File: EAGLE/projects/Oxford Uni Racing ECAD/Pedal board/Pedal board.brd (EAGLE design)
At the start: 165.1 x 114 mm, 50 parts, among them IC1 AD711N, J1 ASS + BOTS, J2 THR_1_2, J3 PWR_CAN, J6 BR_POS_PRESS_STWH, J7 T821108A1S100CEU, K2 EC2-12TNU, T1 BT169, X2 D-SUB9-H2M09ST

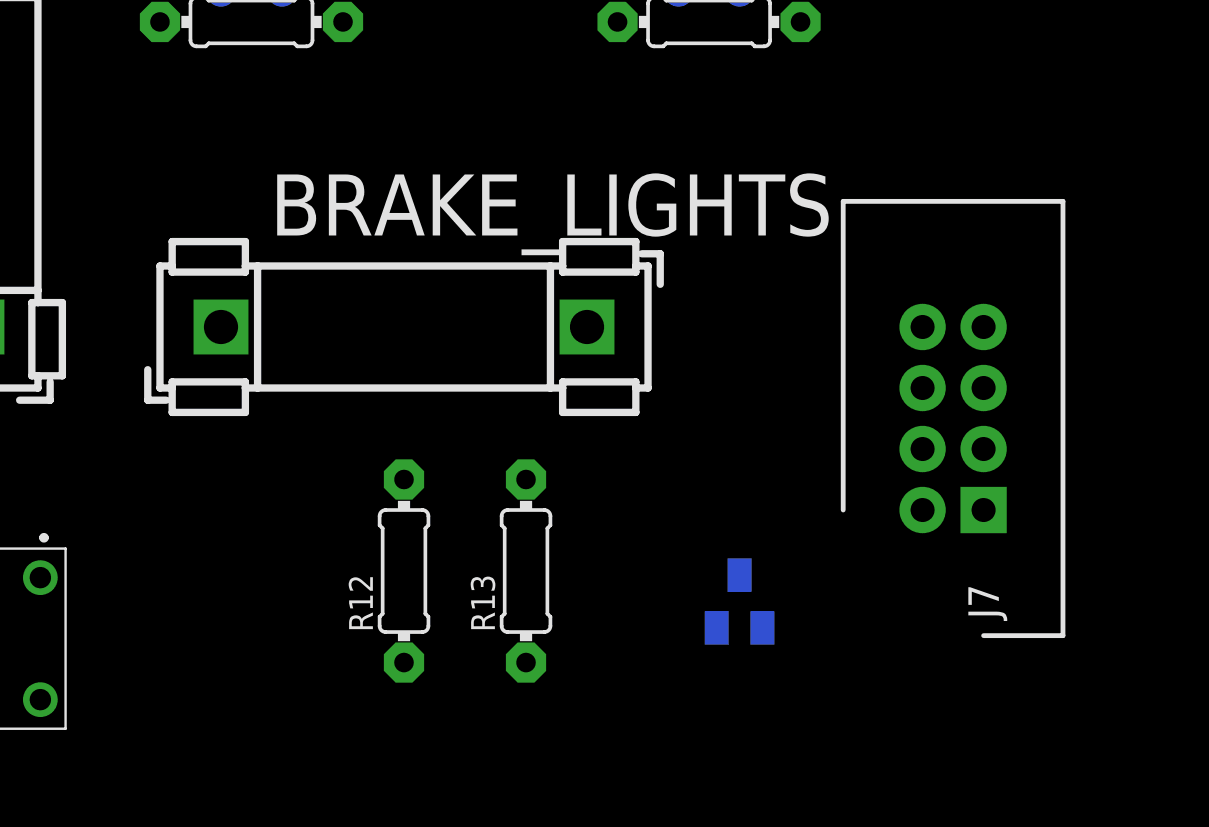
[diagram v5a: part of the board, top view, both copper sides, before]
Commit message: removed brake lights from pedal board
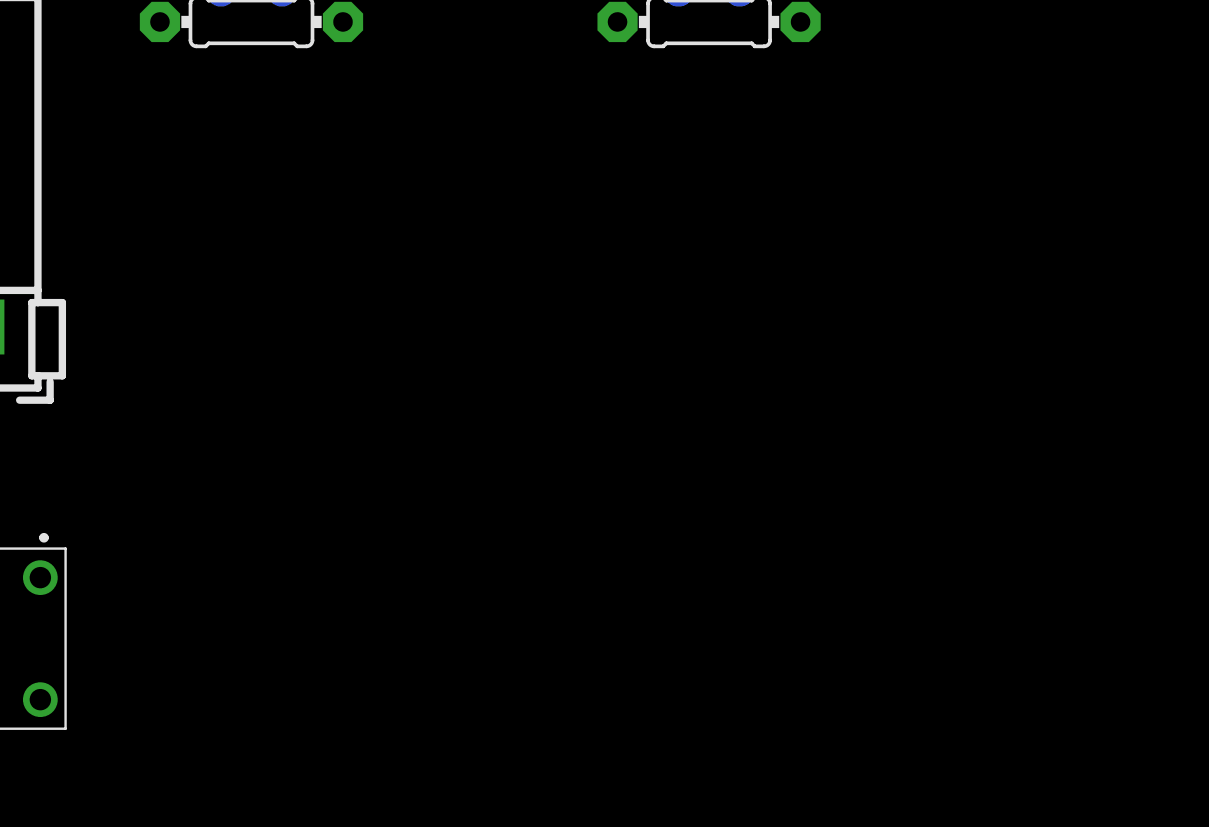
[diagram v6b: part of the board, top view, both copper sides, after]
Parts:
- removed BRAKE_LIGHTS: 1A, fuse:FUSE_HOLDER_5X20MM
- removed BR_LIGHTS_TR: IRLML2502GTRPBF, adafruit:SOT23
- removed J7: T821108A1S100CEU, T821108A1S100CEU:HDRV8W64P254_2X4_1778X895X915P
- removed R12: 1K, adafruit:0204/7
- removed R13: 47K, adafruit:0204/7
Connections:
- removed net 12V_BR_LIGHTS: BRAKE_LIGHTS.2, J7.8
- removed net BRAKE_LIGHTS_OUT: R12.1, U$1.J804-2
- removed net N$25: BR_LIGHTS_TR.1, R12.2, R13.2
- removed net N$28: BR_LIGHTS_TR.3, J7.3
- net 12V_BATTERY: no longer BRAKE_LIGHTS.1
- net BR_POSS2: no longer U$1.J803-3
- net GND: no longer BR_LIGHTS_TR.2, R13.1
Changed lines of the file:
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@@
 <attribute name="VALUE" x="85.09" y="24.13" size="1.27" layer="27" rot="R270" align="center"/>
-</element>
-<element name="J7" library="T821108A1S100CEU" package="HDRV8W64P254_2X4_1778X895X915P" value="T821108A1S100CEU" x="154.94" y="69.85" smashed="yes" rot="R90">
-<attribute name="DESCRIPTION" value="HEADER, VERTICAL, 2.54MM, 8WAY Amphenol T821 Series, 2.54mm Pitch 8 Way 2 Row Straight PCB Header, Solder Termination, 3A" x="154.94" y="67.31" size="1.778" layer="27" rot="R90" display="off"/>
-<attribute name="HEIGHT" value="9.15mm" x="154.94" y="67.31" size="1.778" layer="27" rot="R90" display="off"/>
-<attribute name="MANUFACTURER_NAME" value="Amphenol" x="154.94" y="67.31" size="1.778" layer="27" rot="R90" display="off"/>
-<attribute name="MANUFACTURER_PART_NUMBER" value="T821108A1S100CEU" x="154.94" y="67.31" size="1.778" layer="27" rot="R90" display="off"/>
-<attribute name="NAME" x="154.94" y="66.04" size="1.27" layer="25" rot="R90" align="center"/>
-<attribute name="RS_PART_NUMBER" value="1702738" x="154.94" y="67.31" size="1.778" layer="27" rot="R90" display="off"/>
-<attribute name="VALUE" x="157.48" y="73.66" size="1.27" layer="27" rot="R90" align="center"/>
-</element>
-<element name="R12" library="adafruit" library_urn="urn:adsk.eagle:library:420" package="0204/7" package3d_urn="urn:adsk.eagle:package:6240596/1" value="1K" x="130.81" y="67.31" smashed="yes" rot="R90">
-<attribute name="NAME" x="129.5146" y="64.77" size="0.9906" layer="25" ratio="12" rot="R90"/>
-<attribute name="VALUE" x="131.2926" y="65.6844" size="0.9906" layer="27" ratio="12" rot="R90"/>
-</element>
-<element name="R13" library="adafruit" library_urn="urn:adsk.eagle:library:420" package="0204/7" package3d_urn="urn:adsk.eagle:package:6240596/1" value="47K" x="135.89" y="67.31" smashed="yes" rot="R90">
-<attribute name="NAME" x="134.5946" y="64.77" size="0.9906" layer="25" ratio="12" rot="R90"/>
-<attribute name="VALUE" x="136.3726" y="65.6844" size="0.9906" layer="27" ratio="12" rot="R90"/>
-</element>
-<element name="BR_LIGHTS_TR" library="adafruit" library_urn="urn:adsk.eagle:library:420" package="SOT23" package3d_urn="urn:adsk.eagle:package:6240836/1" value="IRLML2502GTRPBF" x="144.78" y="66.04" smashed="yes" rot="MR0">
-<attribute name="NAME" x="146.685" y="67.945" size="1.27" layer="26" rot="MR0"/>
-<attribute name="VALUE" x="146.685" y="62.865" size="1.27" layer="28" rot="MR0"/>
 </element>
 <element name="IC1" library="analog-devices" library_urn="urn:adsk.eagle:library:102" package="DIL08" package3d_urn="urn:adsk.eagle:package:3915/1" value="AD711N" x="113.03" y="34.29" smashed="yes" rot="R270">
@@
 <attribute name="OC_NEWARK" value="unknown" x="113.03" y="77.47" size="1.778" layer="27" rot="R90" display="off"/>
 <attribute name="VALUE" x="131.318" y="2.032" size="2.54" layer="27" rot="R270"/>
-</element>
-<element name="BRAKE_LIGHTS" library="fuse" library_urn="urn:adsk.eagle:library:233" package="FUSE_HOLDER_5X20MM" package3d_urn="urn:adsk.eagle:package:14079/1" value="1A" x="123.19" y="77.47" smashed="yes">
-<attribute name="MF" value="" x="123.19" y="77.47" size="1.778" layer="27" display="off"/>
-<attribute name="MPN" value="" x="123.19" y="77.47" size="1.778" layer="27" display="off"/>
-<attribute name="NAME" x="125.222" y="81.28" size="2.54" layer="25"/>
-<attribute name="OC_FARNELL" value="unknown" x="123.19" y="77.47" size="1.778" layer="27" display="off"/>
-<attribute name="OC_NEWARK" value="unknown" x="123.19" y="77.47" size="1.778" layer="27" display="off"/>
-<attribute name="VALUE" x="124.968" y="71.628" size="2.54" layer="27"/>
 </element>
 <element name="R1" library="adafruit" library_urn="urn:adsk.eagle:library:420" package="0204/7" package3d_urn="urn:adsk.eagle:package:6240596/1" value="1M" x="104.14" y="43.18" smashed="yes">
@@
 <contactref element="J2" pad="4"/>
 <contactref element="J6" pad="3"/>
-<contactref element="R13" pad="1"/>
-<contactref element="BR_LIGHTS_TR" pad="2"/>
 <contactref element="IC1" pad="4"/>
 <contactref element="R17" pad="1"/>
@@
 <wire x1="186.18835" y1="29.21" x2="188.01714375" y2="26.57855625" width="0" layer="19" extent="16-16"/>
 <wire x1="182.88" y1="32.5657875" x2="182.88" y2="29.21" width="0" layer="19" extent="16-16"/>
-<wire x1="143.83" y1="64.94" x2="179.202075" y2="41.961225" width="0" layer="19" extent="16-16"/>
+<wire x1="144.78" y1="91.44" x2="180.161775" y2="42.920925" width="0" layer="19" extent="16-16"/>
+<wire x1="139.7" y1="90.17" x2="144.78" y2="91.44" width="0" layer="19" extent="16-16"/>
+<wire x1="134.62" y1="104.14" x2="144.78" y2="96.52" width="0" layer="19" extent="16-16"/>
+<wire x1="120.65" y1="90.17" x2="125.73" y2="91.44" width="0" layer="19" extent="16-16"/>
+<wire x1="99.06" y1="105.5624" x2="120.65" y2="90.17" width="0" layer="19" extent="1-1"/>
+<wire x1="87.63" y1="69.85" x2="93.98" y2="91.44" width="0" layer="19" extent="1-1"/>
+<wire x1="87.63" y1="62.23" x2="87.63" y2="69.85" width="0" layer="19" extent="1-1"/>
+<wire x1="87.63" y1="46.99" x2="87.63" y2="62.23" width="0" layer="19" extent="1-1"/>
+<wire x1="90.17" y1="46.99" x2="87.63" y2="46.99" width="0" layer="19" extent="1-1"/>
+<wire x1="87.63" y1="26.67" x2="87.63" y2="46.99" width="0" layer="19" extent="1-1"/>
+<wire x1="105.41" y1="31.75" x2="87.63" y2="26.67" width="0" layer="19" extent="1-1"/>
+<wire x1="109.22" y1="30.48" x2="105.41" y2="31.75" width="0" layer="19" extent="1-1"/>
+<wire x1="63.5" y1="60.96" x2="87.63" y2="62.23" width="0" layer="19" extent="1-1"/>
+<wire x1="63.5" y1="58.42" x2="63.5" y2="60.96" width="0" layer="19" extent="1-1"/>
 </signal>
 <signal name="N$7">
@@
 <wire x1="63.5" y1="45.72" x2="87.63" y2="24.13" width="0" layer="19" extent="1-1"/>
 </signal>
-<signal name="BRAKE_LIGHTS_OUT">
-<contactref element="R12" pad="1"/>
-<contactref element="U$1" pad="J804-2"/>
-<wire x1="15.24" y1="43.18" x2="130.81" y2="63.5" width="0" layer="19" extent="1-1"/>
-</signal>
-<signal name="N$25">
-<contactref element="R12" pad="2"/>
-<contactref element="R13" pad="2"/>
-<contactref element="BR_LIGHTS_TR" pad="1"/>
-<wire x1="135.89" y1="71.12" x2="145.73" y2="64.94" width="0" layer="19" extent="16-16"/>
-<wire x1="130.81" y1="71.12" x2="135.89" y2="71.12" width="0" layer="19" extent="1-1"/>
-</signal>
-<signal name="N$28">
-<contactref element="J7" pad="3"/>
-<contactref element="BR_LIGHTS_TR" pad="3"/>
-<wire x1="144.78" y1="67.14" x2="154.94" y2="72.39" width="0" layer="19" extent="16-16"/>
-</signal>
 <signal name="N$23">
 <contactref element="IC1" pad="6"/>
@@
 <contactref element="J6" pad="7"/>
 <contactref element="R4" pad="1"/>
-<contactref element="U$1" pad="J803-3"/>
 <wire x1="87.63" y1="21.59" x2="100.33" y2="17.78" width="0" layer="19" extent="1-1"/>
-<wire x1="63.5" y1="43.18" x2="87.63" y2="21.59" width="0" layer="19" extent="1-1"/>
 </signal>
 <signal name="ST_WH_POSS">
@@
 <contactref element="J3" pad="2"/>
 <contactref element="F1" pad="1"/>
-<contactref element="BRAKE_LIGHTS" pad="1"/>
-<wire x1="113.03" y1="77.47" x2="123.19" y2="77.47" width="0" layer="19" extent="1-1"/>
 <wire x1="91.44" y1="91.44" x2="113.03" y2="77.47" width="0" layer="19" extent="1-1"/>
 <wire x1="91.44" y1="93.98" x2="91.44" y2="91.44" width="0" layer="19" extent="1-1"/>
 </signal>
-<signal name="12V_BR_LIGHTS">
-<contactref element="J7" pad="8"/>
-<contactref element="BRAKE_LIGHTS" pad="2"/>
-<wire x1="138.43" y1="77.47" x2="152.4" y2="77.47" width="0" layer="19" extent="1-1"/>
-</signal>
 <signal name="N$4">

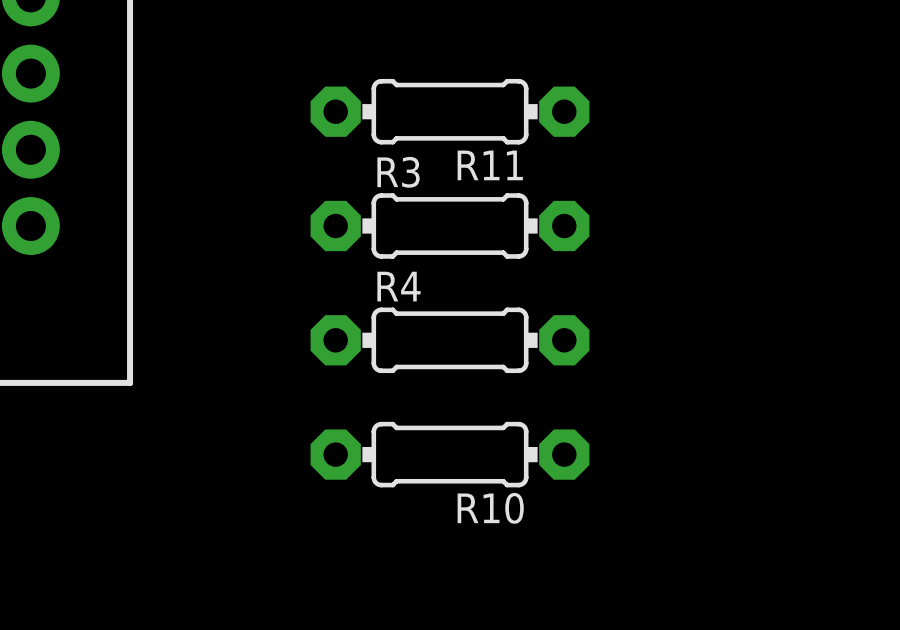
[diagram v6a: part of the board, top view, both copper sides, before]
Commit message: removed brake lights from pedal board
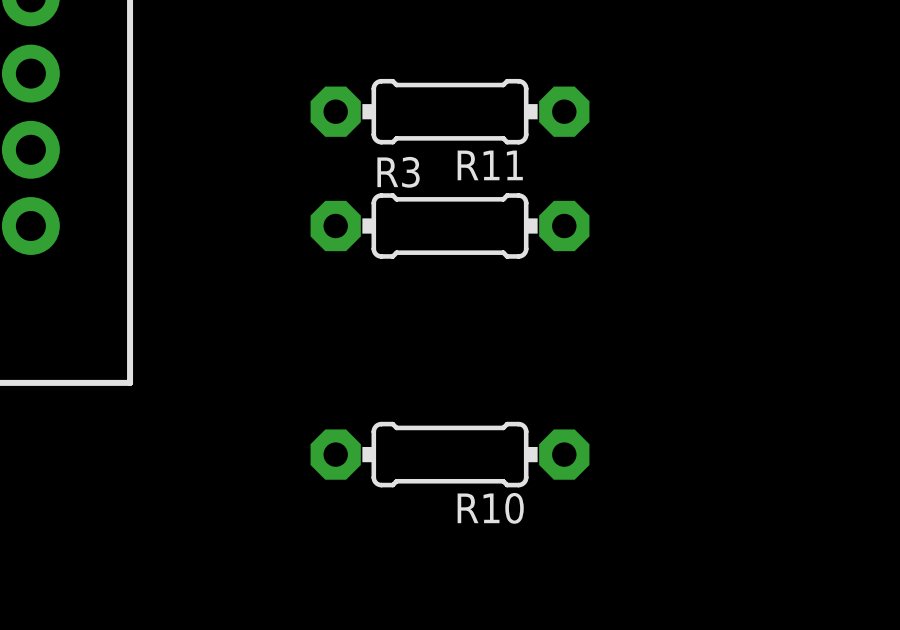
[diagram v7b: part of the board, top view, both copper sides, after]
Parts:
- removed R4: 1M, adafruit:0204/7
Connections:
- removed net BR_POSS2: J6.7, R4.1
- net 5V: no longer R4.2
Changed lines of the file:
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@@
 <attribute name="VALUE" x="102.5144" y="21.1074" size="0.9906" layer="27" ratio="12"/>
-</element>
-<element name="R4" library="adafruit" library_urn="urn:adsk.eagle:library:420" package="0204/7" package3d_urn="urn:adsk.eagle:package:6240596/1" value="1M" x="104.14" y="17.78" smashed="yes">
-<attribute name="NAME" x="101.6" y="19.0754" size="0.9906" layer="25" ratio="12"/>
-<attribute name="VALUE" x="102.5144" y="17.2974" size="0.9906" layer="27" ratio="12"/>
 </element>
 <element name="R10" library="adafruit" library_urn="urn:adsk.eagle:library:420" package="0204/7" package3d_urn="urn:adsk.eagle:package:6240596/1" value="1M" x="104.14" y="13.97" smashed="yes" rot="R180">
@@
 <contactref element="R21" pad="E"/>
 <contactref element="R10" pad="1"/>
-<contactref element="R4" pad="2"/>
 <contactref element="R11" pad="1"/>
 <contactref element="R3" pad="2"/>
@@
 <contactref element="U$1" pad="J802-4"/>
 <wire x1="107.95" y1="13.97" x2="222.885" y2="2.54" width="0" layer="19" extent="1-1"/>
-<wire x1="107.95" y1="17.78" x2="107.95" y2="13.97" width="0" layer="19" extent="1-1"/>
-<wire x1="107.95" y1="21.59" x2="107.95" y2="17.78" width="0" layer="19" extent="1-1"/>
+<wire x1="107.95" y1="21.59" x2="107.95" y2="13.97" width="0" layer="19" extent="1-1"/>
 <wire x1="107.95" y1="25.4" x2="107.95" y2="21.59" width="0" layer="19" extent="1-1"/>
 <wire x1="107.95" y1="43.18" x2="107.95" y2="25.4" width="0" layer="19" extent="1-1"/>
@@
 <wire x1="200.12786875" y1="23.44928125" x2="202.03794375" y2="25.35935625" width="0" layer="19" extent="16-16"/>
 </signal>
-<signal name="BR_POSS2">
-<contactref element="J6" pad="7"/>
-<contactref element="R4" pad="1"/>
-<wire x1="87.63" y1="21.59" x2="100.33" y2="17.78" width="0" layer="19" extent="1-1"/>
-</signal>
 <signal name="ST_WH_POSS">
